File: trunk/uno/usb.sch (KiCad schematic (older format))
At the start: 22 parts, among them U3 ATMEGA16U2-MU(R), X2 USB-B_TH

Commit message: Schematic ERC passes. Circuit _might_ be complete, without errors. You just never know. :-P
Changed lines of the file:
@@
 	1800 4700 1800 5500
 Wire Wire Line
-	1700 4750 1700 5500
+	1700 4700 1700 5500
 Connection ~ 1800 5500
 $Comp
@@
 	9600 5150 9450 5150
 Wire Wire Line
-	10100 5150 10300 5150
+	10300 5150 10100 5150
 Wire Wire Line
-	10300 5150 10300 4350
+	10300 4350 10300 5150
 Wire Wire Line
 	10100 4700 10300 4700

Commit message: Component packages configured.
PCB initial placement.

Some minor typo corrections.
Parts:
- removed X2: USB-B_TH, symbol USB-B_TH
- added X2: USB-MINI-AB, ~, symbol USB-MINI-AB
- C11, C7, C8, C9: footprint ~ -> SM0603_Capa
- D3: value DIODE -> CD1206-S01575; footprint ~ -> SM1206D
- F1: value 500mA -> MF-MSMF050-2 500mA; footprint ~ -> SM1812
- ISCP1: footprint (none) -> pin_array_3x2
- JP1: value JUMPER -> GROUND; footprint ~ -> JSOLD
- JP2: footprint (none) -> PIN_ARRAY_2X2
- L1: footprint ~ -> SM0805
- LED3, LED4, RN1C1, RN2B1, RN2C1, RN3A1, RN3D1, XT1: footprint ~ -> (none)
- Z1, Z2: value 5V -> CG0603MLC-05E 5V; footprint ~ -> (none)
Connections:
- wire segments 93 -> 95
- no-connect marks 9 -> 10
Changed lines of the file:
@@
 Sheet 2 3
 Title "KiCADuino UNO Rev3"
-Date "24 jul 2013"
+Date "25 jul 2013"
 Rev "0.1"
 Comp "Gruvin & Co"
@@
 F 0 "U3" H 5900 5500 47  0000 L BNN
 F 1 "ATMEGA16U2-MU(R)" H 6750 2600 47  0000 L BNN
-F 2 "QFN32" H 6600 4000 59  0000 C CNB
+F 2 "QFN32" H 6600 4000 59  0001 C CNB
 F 3 "~" H 6600 4000 60  0000 C CNN
 	1    6600 4000
@@
 F 0 "XT1" H 4550 3500 60  0000 C CNN
 F 1 "16MHz" H 4750 3250 60  0000 C CNN
-F 2 "~" H 4750 3400 60  0000 C CNN
+F 2 "" H 4750 3400 60  0001 C CNN
 F 3 "~" H 4750 3400 60  0000 C CNN
 	1    4750 3400
@@
 F 0 "C9" H 4400 3800 40  0000 L CNN
 F 1 "22p" H 4406 3615 40  0000 L CNN
-F 2 "~" H 4438 3550 30  0000 C CNN
+F 2 "SM0603_Capa" H 4438 3550 30  0001 C CNN
 F 3 "~" H 4400 3700 60  0000 C CNN
 	1    4400 3700
@@
 F 0 "C11" H 5100 3800 40  0000 L CNN
 F 1 "22p" H 5106 3615 40  0000 L CNN
-F 2 "~" H 5138 3550 30  0000 C CNN
+F 2 "SM0603_Capa" H 5138 3550 30  0001 C CNN
 F 3 "~" H 5100 3700 60  0000 C CNN
 	1    5100 3700
@@
 P 4950 5200
 F 0 "JP1" H 4950 5350 60  0000 C CNN
-F 1 "JUMPER" H 4950 5120 40  0000 C CNN
-F 2 "~" H 4950 5200 60  0000 C CNN
+F 1 "GROUND" H 4950 5120 40  0000 C CNN
+F 2 "JSOLD" H 4950 5200 60  0001 C CNN
 F 3 "~" H 4950 5200 60  0000 C CNN
 	1    4950 5200
@@
 F 0 "ISCP1" H 4650 2400 50  0000 C CNN
 F 1 "3X2 M" H 4650 2000 40  0000 C CNN
-F 2 "" H 4650 2150 60  0000 C CNN
+F 2 "pin_array_3x2" H 4650 2150 60  0001 C CNN
 F 3 "" H 4650 2150 60  0000 C CNN
 	1    4650 2150
@@
 F 0 "RN1C1" V 5400 2500 40  0000 C CNN
 F 1 "10K" V 5307 2501 40  0000 C CNN
-F 2 "~" V 5230 2500 30  0000 C CNN
+F 2 "" V 5230 2500 30  0001 C CNN
 F 3 "~" H 5300 2500 30  0000 C CNN
 	1    5300 2500
@@
 U 1 1 51EFF1FE
 P 5500 2500
-F 0 "D3" H 5550 2400 40  0000 C CNN
-F 1 "DIODE" H 5350 2400 40  0000 C CNN
-F 2 "~" H 5500 2500 60  0000 C CNN
+F 0 "D3" H 5500 2300 40  0000 C CNN
+F 1 "CD1206-S01575" H 5450 2400 40  0000 C CNN
+F 2 "SM1206D" H 5500 2500 60  0001 C CNN
 F 3 "~" H 5500 2500 60  0000 C CNN
 	1    5500 2500
@@
 F 0 "JP2" V 8050 1950 50  0000 L CNN
 F 1 "2X2 M" V 7950 1950 40  0000 L CNN
-F 2 "" H 8000 1800 60  0000 C CNN
+F 2 "PIN_ARRAY_2X2" H 8000 1800 60  0001 C CNN
 F 3 "" H 8000 1800 60  0000 C CNN
 	1    8000 1800
@@
 F 0 "LED3" H 9250 4800 50  0000 C CNN
 F 1 "YELLOW" H 9250 4550 50  0000 C CNN
-F 2 "~" H 9250 4700 60  0000 C CNN
+F 2 "" H 9250 4700 60  0001 C CNN
 F 3 "~" H 9250 4700 60  0000 C CNN
 	1    9250 4700
@@
 F 0 "LED4" H 9250 5250 50  0000 C CNN
 F 1 "YELLOW" H 9250 5000 50  0000 C CNN
-F 2 "~" H 9250 5150 60  0000 C CNN
+F 2 "" H 9250 5150 60  0001 C CNN
 F 3 "~" H 9250 5150 60  0000 C CNN
 	1    9250 5150
@@
 TXD
 $Comp
-L USB-B_TH X2
-U 1 1 51EFFF4B
-P 1800 4350
-F 0 "X2" H 1850 4650 60  0000 C CNN
-F 1 "USB-B_TH" H 1650 4750 60  0000 C CNN
-F 2 "" H 1800 4350 60  0000 C CNN
-F 3 "" H 1800 4350 60  0000 C CNN
-	1    1800 4350
-	1    0    0    -1
-$EndComp
-$Comp
 L VARISTOR Z1
 U 1 1 51F00052
 P 2750 5150
 F 0 "Z1" V 2830 5150 40  0000 C CNN
-F 1 "5V" V 2650 5100 40  0000 L CNN
-F 2 "~" V 2680 5150 30  0000 C CNN
+F 1 "CG0603MLC-05E 5V" V 2600 4900 40  0000 L CNN
+F 2 "" V 2680 5150 30  0001 C CNN
 F 3 "~" H 2750 5150 30  0000 C CNN
 	1    2750 5150
@@
 P 3100 4950
 F 0 "Z2" V 3180 4950 40  0000 C CNN
-F 1 "5V" V 3000 4900 40  0000 L CNN
-F 2 "~" V 3030 4950 30  0000 C CNN
+F 1 "CG0603MLC-05E 5V" V 2950 4700 40  0000 L CNN
+F 2 "" V 3030 4950 30  0001 C CNN
 F 3 "~" H 3100 4950 30  0000 C CNN
 	1    3100 4950
@@
 F 0 "RN3A1" V 3750 4200 40  0000 C CNN
 F 1 "22R" V 3657 4201 40  0000 C CNN
-F 2 "~" V 3580 4200 30  0000 C CNN
+F 2 "" V 3580 4200 30  0001 C CNN
 F 3 "~" H 3650 4200 30  0000 C CNN
 	1    3650 4200
@@
 F 0 "RN3D1" V 3750 4500 40  0000 C CNN
 F 1 "22R" V 3657 4501 40  0000 C CNN
-F 2 "~" V 3580 4500 30  0000 C CNN
+F 2 "" V 3580 4500 30  0001 C CNN
 F 3 "~" H 3650 4500 30  0000 C CNN
 	1    3650 4500
@@
 F 0 "L1" V 2830 5900 40  0000 C CNN
 F 1 "FERRITE" V 2650 5800 40  0000 L CNN
-F 2 "~" V 2680 5900 30  0000 C CNN
+F 2 "SM0805" V 2680 5900 30  0001 C CNN
 F 3 "~" H 2750 5900 30  0000 C CNN
 	1    2750 5900
@@
 Wire Wire Line
 	3100 5500 3100 5200
-Wire Wire Line
-	1700 5500 3100 5500
 Connection ~ 2750 5500
 Wire Wire Line
@@
 F 0 "C8" H 4150 5200 40  0000 L CNN
 F 1 "1u" H 4156 5015 40  0000 L CNN
-F 2 "~" H 4188 4950 30  0000 C CNN
+F 2 "SM0603_Capa" H 4188 4950 30  0001 C CNN
 F 3 "~" H 4150 5100 60  0000 C CNN
 	1    4150 5100
@@
 F 0 "C7" H 5200 4350 40  0000 L CNN
 F 1 "100n" H 5206 4165 40  0000 L CNN
-F 2 "~" H 5238 4100 30  0000 C CNN
+F 2 "SM0603_Capa" H 5238 4100 30  0001 C CNN
 F 3 "~" H 5200 4250 60  0000 C CNN
 	1    5200 4250
@@
 	5200 4000 5450 4000
 Connection ~ 5450 4000
-Wire Wire Line
-	2050 4500 2300 4500
-Wire Wire Line
-	2300 4500 2300 6250
-Wire Wire Line
-	2300 6250 2750 6250
 Connection ~ 2750 6250
-Wire Wire Line
-	1800 4700 1800 5500
-Wire Wire Line
-	1700 4700 1700 5500
-Connection ~ 1800 5500
 $Comp
 L FUSE F1
 U 1 1 51F00975
 P 2850 3900
-F 0 "F1" H 2950 3950 40  0000 C CNN
-F 1 "500mA" H 2750 3850 40  0000 C CNN
-F 2 "~" H 2850 3900 60  0000 C CNN
+F 0 "F1" H 2750 3850 40  0000 C CNN
+F 1 "MF-MSMF050-2 500mA" H 2800 4000 40  0000 C CNN
+F 2 "SM1812" H 2850 3900 60  0001 C CNN
 F 3 "~" H 2850 3900 60  0000 C CNN
 	1    2850 3900
@@
 F 0 "RN2C1" V 9950 4700 40  0000 C CNN
 F 1 "1K" V 9857 4701 40  0000 C CNN
-F 2 "~" V 9780 4700 30  0000 C CNN
+F 2 "" V 9780 4700 30  0001 C CNN
 F 3 "~" H 9850 4700 30  0000 C CNN
 	1    9850 4700
@@
 F 0 "RN2B1" V 9950 5150 40  0000 C CNN
 F 1 "1K" V 9857 5151 40  0000 C CNN
-F 2 "~" V 9780 5150 30  0000 C CNN
+F 2 "" V 9780 5150 30  0001 C CNN
 F 3 "~" H 9850 5150 30  0000 C CNN
 	1    9850 5150
@@
 	3850 3500 4000 3500
 Connection ~ 4000 3900
+$Comp
+L USB-MINI-AB X2
+U 1 1 51F0FF25
+P 1800 4400
+F 0 "X2" H 1900 4750 60  0000 C CNN
+F 1 "USB-MINI-AB" H 1400 4750 60  0000 C CNN
+F 2 "~" H 1800 4400 60  0000 C CNN
+F 3 "~" H 1800 4400 60  0000 C CNN
+	1    1800 4400
+	1    0    0    -1
+$EndComp
+Wire Wire Line
+	1350 5500 3100 5500
+Wire Wire Line
+	2750 6250 2200 6250
+Wire Wire Line
+	2200 6250 2200 4600
+Wire Wire Line
+	2200 4600 2050 4600
+Wire Wire Line
+	1650 4800 1650 5500
+Wire Wire Line
+	1550 4800 1550 5500
+Connection ~ 1650 5500
+Wire Wire Line
+	1450 4800 1450 5500
+Connection ~ 1550 5500
+Wire Wire Line
+	1350 4800 1350 5500
+Connection ~ 1450 5500
+NoConn ~ 2050 4500
 $EndSCHEMATC

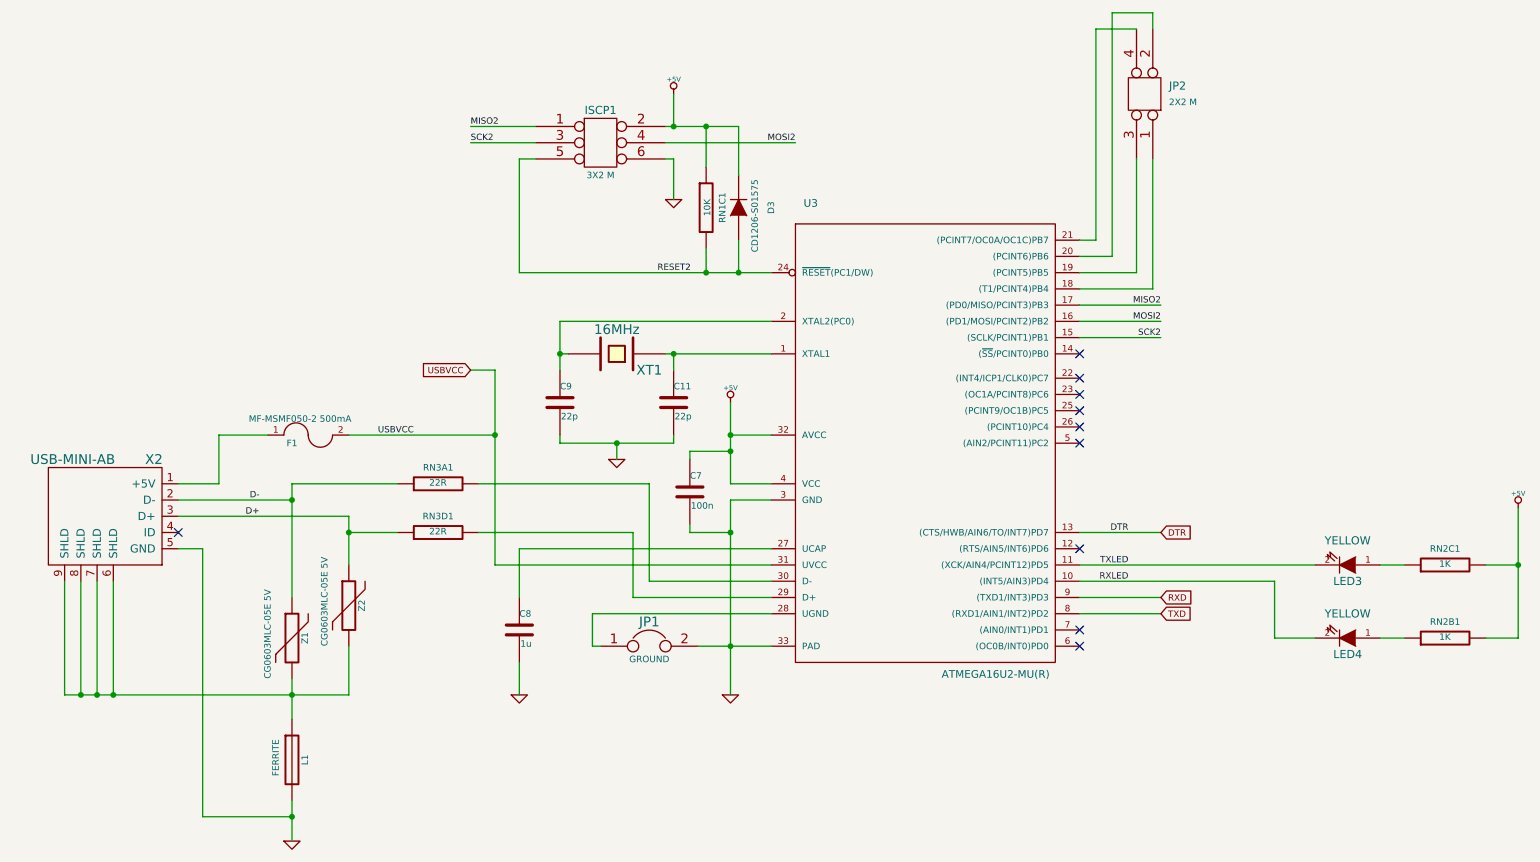
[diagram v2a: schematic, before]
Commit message: Added resistor network part/module for RN1-4 (no 3D package yet).
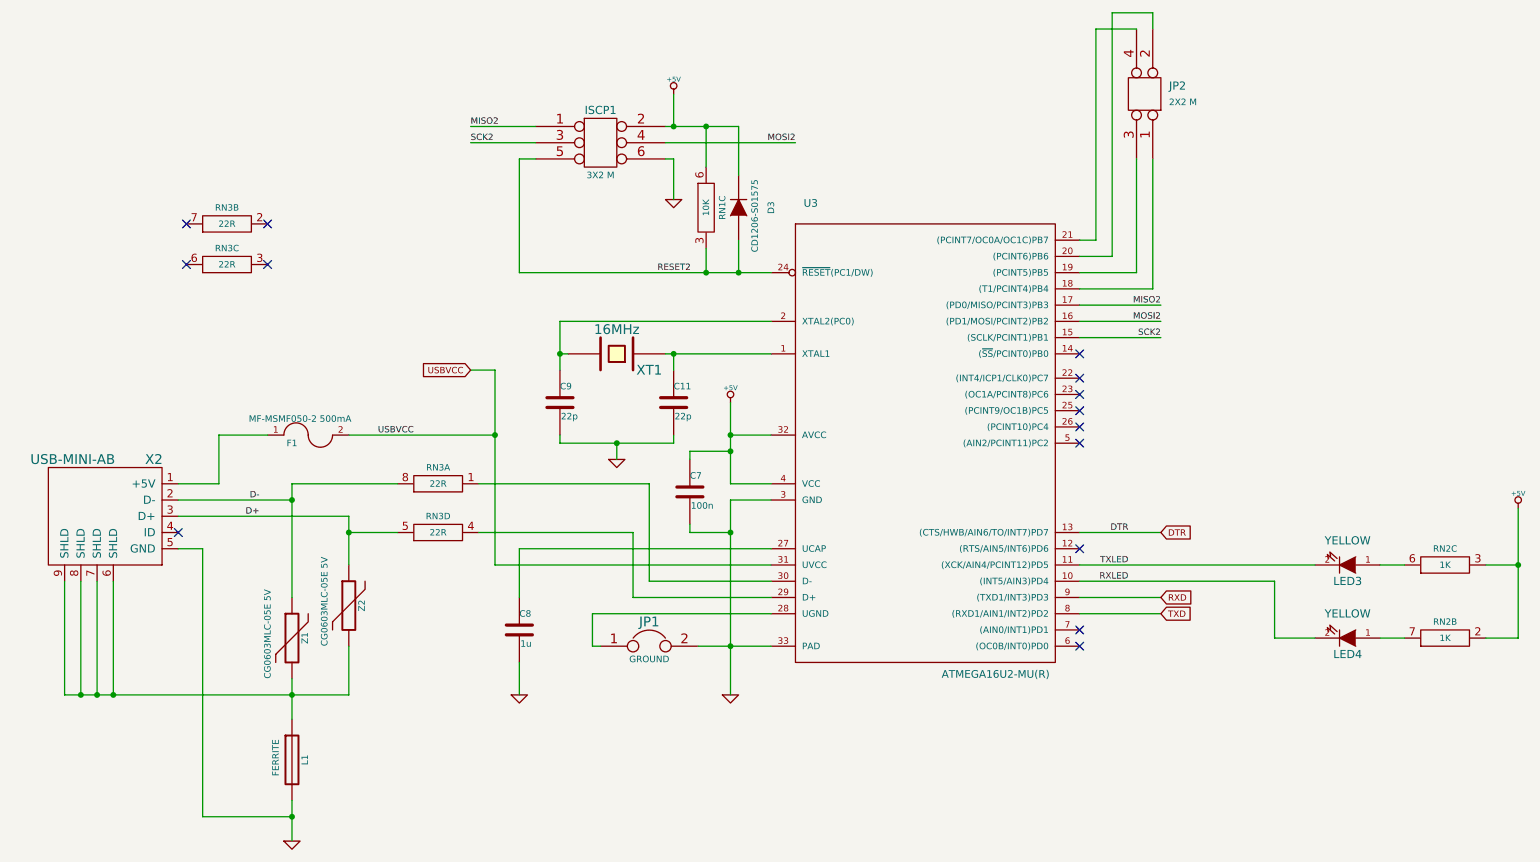
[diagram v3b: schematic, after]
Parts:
- removed RN1C1: 10K, symbol R
- removed RN2B1, RN2C1: 1K, symbol R
- removed RN3A1, RN3D1: 22R, symbol R
- added RN1: 10K, symbol R_NET4
- added RN2: 1K, symbol R_NET4
- added RN3: 22R, symbol R_NET4
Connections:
- net +5V: now also RN1.6, RN2.2 (3), RN2.3
- net D+: now also RN3.5 (6)
- net D-: now also RN3.8 (6)
- net RESET2: now also RN1.3
- net at U3.29 (D+): now also RN3.4 (3)
- net at U3.30 (D-): now also RN3.1 (3)
- net at LED3.1 (A): now also RN2.6
- net at LED4.1 (A): now also RN2.7 (6)
- no-connect marks 10 -> 14
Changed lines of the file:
@@
 MISO2
-$Comp
-L R RN1C1
-U 1 1 51EFF1A1
-P 5300 2500
-F 0 "RN1C1" V 5400 2500 40  0000 C CNN
-F 1 "10K" V 5307 2501 40  0000 C CNN
-F 2 "" V 5230 2500 30  0001 C CNN
-F 3 "~" H 5300 2500 30  0000 C CNN
-	1    5300 2500
-	1    0    0    -1
-$EndComp
 $Comp
 L DIODE D3
@@
 $EndComp
 $Comp
-L R RN3A1
-U 1 1 51F0007E
-P 3650 4200
-F 0 "RN3A1" V 3750 4200 40  0000 C CNN
-F 1 "22R" V 3657 4201 40  0000 C CNN
-F 2 "" V 3580 4200 30  0001 C CNN
-F 3 "~" H 3650 4200 30  0000 C CNN
-	1    3650 4200
-	0    -1   -1   0
-$EndComp
-$Comp
-L R RN3D1
-U 1 1 51F00084
-P 3650 4500
-F 0 "RN3D1" V 3750 4500 40  0000 C CNN
-F 1 "22R" V 3657 4501 40  0000 C CNN
-F 2 "" V 3580 4500 30  0001 C CNN
-F 3 "~" H 3650 4500 30  0000 C CNN
-	1    3650 4500
-	0    -1   -1   0
-$EndComp
-$Comp
 L GND #PWR017
 U 1 1 51F000AD
@@
 Wire Wire Line
 	4000 3900 3100 3900
-$Comp
-L R RN2C1
-U 1 1 51F00E41
-P 9850 4700
-F 0 "RN2C1" V 9950 4700 40  0000 C CNN
-F 1 "1K" V 9857 4701 40  0000 C CNN
-F 2 "" V 9780 4700 30  0001 C CNN
-F 3 "~" H 9850 4700 30  0000 C CNN
-	1    9850 4700
-	0    -1   -1   0
-$EndComp
-$Comp
-L R RN2B1
-U 1 1 51F00E4C
-P 9850 5150
-F 0 "RN2B1" V 9950 5150 40  0000 C CNN
-F 1 "1K" V 9857 5151 40  0000 C CNN
-F 2 "" V 9780 5150 30  0001 C CNN
-F 3 "~" H 9850 5150 30  0000 C CNN
-	1    9850 5150
-	0    -1   -1   0
-$EndComp
 Wire Wire Line
 	9600 4700 9450 4700
@@
 Connection ~ 1450 5500
 NoConn ~ 2050 4500
+$Comp
+L R_NET4 RN1
+U 3 1 51F111DF
+P 5300 2500
+F 0 "RN1" V 5400 2500 39  0000 C CNN
+F 1 "10K" V 5300 2500 39  0000 C CNN
+F 2 "" H 5300 2500 60  0000 C CNN
+F 3 "" H 5300 2500 60  0000 C CNN
+	3    5300 2500
+	1    0    0    -1
+$EndComp
+$Comp
+L R_NET4 RN2
+U 3 1 51F1185C
+P 9850 4700
+F 0 "RN2" V 9950 4700 39  0000 C CNN
+F 1 "1K" V 9850 4700 39  0000 C CNN
+F 2 "" H 9850 4700 60  0000 C CNN
+F 3 "" H 9850 4700 60  0000 C CNN
+	3    9850 4700
+	0    -1   -1   0
+$EndComp
+$Comp
+L R_NET4 RN2
+U 2 1 51F1188E
+P 9850 5150
+F 0 "RN2" V 9950 5150 39  0000 C CNN
+F 1 "1K" V 9850 5150 39  0000 C CNN
+F 2 "" H 9850 5150 60  0000 C CNN
+F 3 "" H 9850 5150 60  0000 C CNN
+	2    9850 5150
+	0    -1   -1   0
+$EndComp
+$Comp
+L R_NET4 RN3
+U 1 1 51F11CEF
+P 3650 4200
+F 0 "RN3" V 3750 4200 39  0000 C CNN
+F 1 "22R" V 3650 4200 39  0000 C CNN
+F 2 "" H 3650 4200 60  0000 C CNN
+F 3 "" H 3650 4200 60  0000 C CNN
+	1    3650 4200
+	0    -1   -1   0
+$EndComp
+$Comp
+L R_NET4 RN3
+U 4 1 51F11CFC
+P 3650 4500
+F 0 "RN3" V 3750 4500 39  0000 C CNN
+F 1 "22R" V 3650 4500 39  0000 C CNN
+F 2 "" H 3650 4500 60  0000 C CNN
+F 3 "" H 3650 4500 60  0000 C CNN
+	4    3650 4500
+	0    -1   -1   0
+$EndComp
+$Comp
+L R_NET4 RN3
+U 2 1 51F11D5C
+P 2350 2600
+F 0 "RN3" V 2450 2600 39  0000 C CNN
+F 1 "22R" V 2350 2600 39  0000 C CNN
+F 2 "" H 2350 2600 60  0000 C CNN
+F 3 "" H 2350 2600 60  0000 C CNN
+	2    2350 2600
+	0    -1   -1   0
+$EndComp
+$Comp
+L R_NET4 RN3
+U 3 1 51F11D62
+P 2350 2850
+F 0 "RN3" V 2450 2850 39  0000 C CNN
+F 1 "22R" V 2350 2850 39  0000 C CNN
+F 2 "" H 2350 2850 60  0000 C CNN
+F 3 "" H 2350 2850 60  0000 C CNN
+	3    2350 2850
+	0    -1   -1   0
+$EndComp
+NoConn ~ 2600 2600
+NoConn ~ 2600 2850
+NoConn ~ 2100 2850
+NoConn ~ 2100 2600
 $EndSCHEMATC

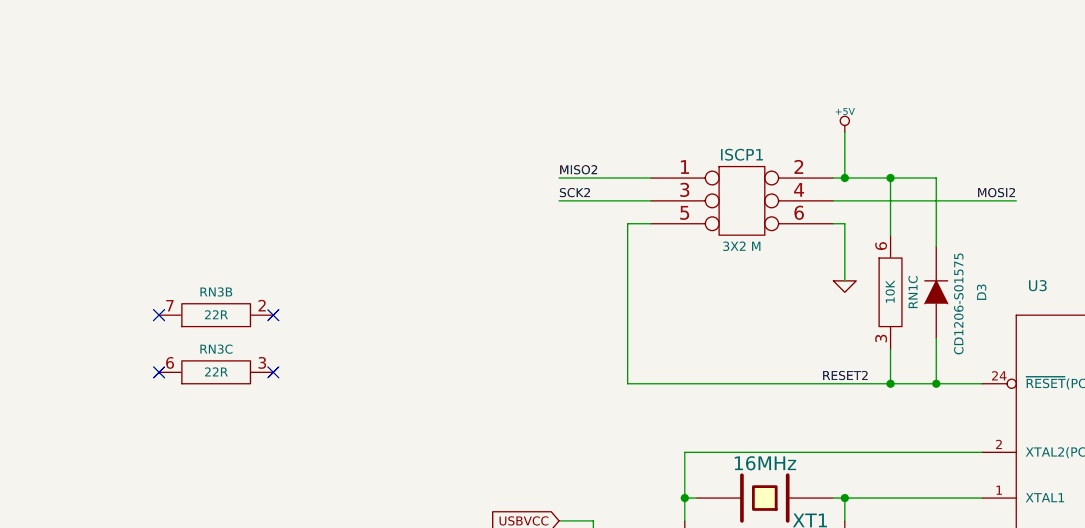
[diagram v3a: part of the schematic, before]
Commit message: About half the comoponents placed, in the exact same location as the UNO Rev3 reference design, except I changed the USB socket to a mini.
A number of minor schematic errors were corrected, around the pin 
numbering of the four resistor network chips.
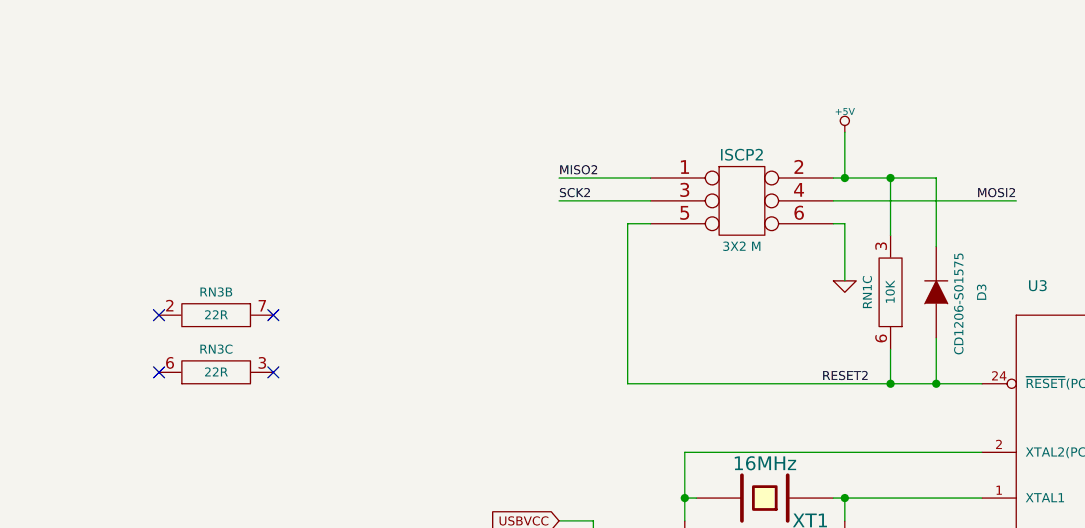
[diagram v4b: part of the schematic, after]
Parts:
- renumbered ISCP1 to ISCP2
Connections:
- net +5V: now also RN1.3; no longer RN1.6
- net RESET2: now also RN1.6; no longer RN1.3
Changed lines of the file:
@@
 $EndComp
 $Comp
-L CONN_3X2 ISCP1
+L CONN_3X2 ISCP2
 U 1 1 51EFEEEB
 P 4650 2150
-F 0 "ISCP1" H 4650 2400 50  0000 C CNN
+F 0 "ISCP2" H 4650 2400 50  0000 C CNN
 F 1 "3X2 M" H 4650 2000 40  0000 C CNN
 F 2 "pin_array_3x2" H 4650 2150 60  0001 C CNN
@@
 F 3 "" H 5300 2500 60  0000 C CNN
 	3    5300 2500
-	1    0    0    -1
+	-1   0    0    1
 $EndComp
 $Comp
@@
 U 2 1 51F11D5C
 P 2350 2600
-F 0 "RN3" V 2450 2600 39  0000 C CNN
+F 0 "RN3" V 2250 2600 39  0000 C CNN
 F 1 "22R" V 2350 2600 39  0000 C CNN
 F 2 "" H 2350 2600 60  0000 C CNN
 F 3 "" H 2350 2600 60  0000 C CNN
 	2    2350 2600
-	0    -1   -1   0
-$EndComp
-$Comp
+	0    1    1    0
+$EndComp
+$Comp
